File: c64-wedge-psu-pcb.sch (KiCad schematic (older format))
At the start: 15 parts, among them U1 LM2576T-5

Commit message: Make R1 pads bigger
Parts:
- R1: footprint Resistor_THT:R_Axial_DIN0207_L6.3mm_D2.5mm_P7.62mm_Horizontal -> Resistor_THT:R_Axial_DIN0411_L9.9mm_D3.6mm_P7.62mm_Vertical
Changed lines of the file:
@@
 F 0 "R1" V 5543 3650 50  0000 C CNN
 F 1 "0R" V 5634 3650 50  0000 C CNN
-F 2 "Resistor_THT:R_Axial_DIN0207_L6.3mm_D2.5mm_P7.62mm_Horizontal" V 5680 3650 50  0001 C CNN
+F 2 "Resistor_THT:R_Axial_DIN0411_L9.9mm_D3.6mm_P7.62mm_Vertical" V 5680 3650 50  0001 C CNN
 F 3 "~" H 5750 3650 50  0001 C CNN
 	1    5750 3650

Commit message: relayout, change some values and footprints
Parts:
- C1, C2: footprint Capacitor_THT:CP_Radial_D18.0mm_P7.50mm -> Capacitor_THT:CP_Radial_D16.0mm_P7.50mm
- C3: footprint Capacitor_THT:CP_Radial_D6.3mm_P2.50mm -> Capacitor_THT:CP_Radial_D8.0mm_P3.50mm
- L2: renamed from L3; value 22uH -> 20uH; footprint Inductor_THT:L_Toroid_Vertical_L19.1mm_W8.1mm_P7.10mm_Bourns_5700 -> Inductor_THT:L_Toroid_Vertical_L16.0mm_W8.0mm_P7.62mm
- R1: footprint Resistor_THT:R_Axial_DIN0411_L9.9mm_D3.6mm_P7.62mm_Vertical -> Resistor_THT:R_Axial_DIN0411_L9.9mm_D3.6mm_P5.08mm_Vertical
- U1: footprint Package_TO_SOT_THT:TO-220-5_P3.4x3.8mm_StaggerEven_Lead7.13mm_TabDown -> Package_TO_SOT_THT:TO-220-5_P3.4x3.7mm_StaggerEven_Lead3.8mm_Vertical
- renumbered L2 to L1
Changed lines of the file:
@@
 F 0 "U1" H 4600 4117 50  0000 C CNN
 F 1 "LM2576T-5" H 4600 4026 50  0000 C CNN
-F 2 "Package_TO_SOT_THT:TO-220-5_P3.4x3.8mm_StaggerEven_Lead7.13mm_TabDown" H 4600 3500 50  0001 L CIN
+F 2 "Package_TO_SOT_THT:TO-220-5_P3.4x3.7mm_StaggerEven_Lead3.8mm_Vertical" H 4600 3500 50  0001 L CIN
 F 3 "http://www.ti.com/lit/ds/symlink/lm2576.pdf" H 4600 3750 50  0001 C CNN
 	1    4600 3750
@@
 $EndComp
 $Comp
-L Device:L L2
+L Device:L L1
 U 1 1 5F7EB0E4
 P 5750 3850
-F 0 "L2" V 5662 3850 50  0000 C CNN
+F 0 "L1" V 5662 3850 50  0000 C CNN
 F 1 "150uH" V 5571 3850 50  0000 C CNN
 F 2 "Inductor_THT:L_Toroid_Vertical_L24.6mm_W15.5mm_P11.44mm_Pulse_KM-4" H 5750 3850 50  0001 C CNN
@@
 F 0 "C2" H 6218 4046 50  0000 L CNN
 F 1 "2200uF" H 6218 3955 50  0000 L CNN
-F 2 "Capacitor_THT:CP_Radial_D18.0mm_P7.50mm" H 6138 3850 50  0001 C CNN
+F 2 "Capacitor_THT:CP_Radial_D16.0mm_P7.50mm" H 6138 3850 50  0001 C CNN
 F 3 "~" H 6100 4000 50  0001 C CNN
 	1    6100 4000
@@
 F 0 "R1" V 5543 3650 50  0000 C CNN
 F 1 "0R" V 5634 3650 50  0000 C CNN
-F 2 "Resistor_THT:R_Axial_DIN0411_L9.9mm_D3.6mm_P7.62mm_Vertical" V 5680 3650 50  0001 C CNN
+F 2 "Resistor_THT:R_Axial_DIN0411_L9.9mm_D3.6mm_P5.08mm_Vertical" V 5680 3650 50  0001 C CNN
 F 3 "~" H 5750 3650 50  0001 C CNN
 	1    5750 3650
@@
 F 0 "C1" H 3668 3996 50  0000 L CNN
 F 1 "4700uF" H 3668 3905 50  0000 L CNN
-F 2 "Capacitor_THT:CP_Radial_D18.0mm_P7.50mm" H 3588 3800 50  0001 C CNN
+F 2 "Capacitor_THT:CP_Radial_D16.0mm_P7.50mm" H 3588 3800 50  0001 C CNN
 F 3 "~" H 3550 3950 50  0001 C CNN
 	1    3550 3950
@@
 F 0 "C3" H 7365 3996 50  0000 L CNN
 F 1 "100uF" H 7365 3905 50  0000 L CNN
-F 2 "Capacitor_THT:CP_Radial_D6.3mm_P2.50mm" H 7288 3800 50  0001 C CNN
+F 2 "Capacitor_THT:CP_Radial_D8.0mm_P3.50mm" H 7288 3800 50  0001 C CNN
 F 3 "~" H 7250 3950 50  0001 C CNN
 	1    7250 3950
@@
 $EndComp
 $Comp
-L Device:L L3
+L Device:L L2
 U 1 1 5F85825E
 P 6900 3650
-F 0 "L3" V 7090 3650 50  0000 C CNN
-F 1 "22uH" V 6999 3650 50  0000 C CNN
-F 2 "Inductor_THT:L_Toroid_Vertical_L19.1mm_W8.1mm_P7.10mm_Bourns_5700" H 6900 3650 50  0001 C CNN
+F 0 "L2" V 7090 3650 50  0000 C CNN
+F 1 "20uH" V 6999 3650 50  0000 C CNN
+F 2 "Inductor_THT:L_Toroid_Vertical_L16.0mm_W8.0mm_P7.62mm" H 6900 3650 50  0001 C CNN
 F 3 "~" H 6900 3650 50  0001 C CNN
 	1    6900 3650

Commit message: Modify footprints, add some info text, modify resistor values
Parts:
- C3: value 100uF -> 220uF 50V; symbol Device:C -> Device:CP
- R1: value 0R -> 200R
- R2: value 330R -> 200R
- U1: footprint Package_TO_SOT_THT:TO-220-5_P3.4x3.7mm_StaggerEven_Lead3.8mm_Vertical -> Package_TO_SOT_THT:TO-220-5_P3.4x3.8mm_StaggerEven_Lead7.13mm_TabDown
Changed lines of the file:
@@
 F 0 "U1" H 4600 4117 50  0000 C CNN
 F 1 "LM2576T-5" H 4600 4026 50  0000 C CNN
-F 2 "Package_TO_SOT_THT:TO-220-5_P3.4x3.7mm_StaggerEven_Lead3.8mm_Vertical" H 4600 3500 50  0001 L CIN
+F 2 "Package_TO_SOT_THT:TO-220-5_P3.4x3.8mm_StaggerEven_Lead7.13mm_TabDown" H 4600 3500 50  0001 L CIN
 F 3 "http://www.ti.com/lit/ds/symlink/lm2576.pdf" H 4600 3750 50  0001 C CNN
 	1    4600 3750
@@
 P 8250 4000
 F 0 "R2" V 8457 4000 50  0000 C CNN
-F 1 "330R" V 8366 4000 50  0000 C CNN
+F 1 "200R" V 8366 4000 50  0000 C CNN
 F 2 "Resistor_THT:R_Axial_DIN0207_L6.3mm_D2.5mm_P7.62mm_Horizontal" V 8180 4000 50  0001 C CNN
 F 3 "~" H 8250 4000 50  0001 C CNN
@@
 $EndComp
 Wire Wire Line
-	7250 4250 8450 4250
-Wire Wire Line
 	8450 3650 8450 4000
 Wire Wire Line
@@
 P 5750 3650
 F 0 "R1" V 5543 3650 50  0000 C CNN
-F 1 "0R" V 5634 3650 50  0000 C CNN
+F 1 "200R" V 5634 3650 50  0000 C CNN
 F 2 "Resistor_THT:R_Axial_DIN0411_L9.9mm_D3.6mm_P5.08mm_Vertical" V 5680 3650 50  0001 C CNN
 F 3 "~" H 5750 3650 50  0001 C CNN
@@
 	3550 3650 3550 3800
 $Comp
-L Device:C C3
+L Device:CP C3
 U 1 1 5F8576FF
-P 7250 3950
-F 0 "C3" H 7365 3996 50  0000 L CNN
-F 1 "100uF" H 7365 3905 50  0000 L CNN
-F 2 "Capacitor_THT:CP_Radial_D8.0mm_P3.50mm" H 7288 3800 50  0001 C CNN
-F 3 "~" H 7250 3950 50  0001 C CNN
-	1    7250 3950
+P 7150 3950
+F 0 "C3" H 7265 3996 50  0000 L CNN
+F 1 "220uF 50V" H 7265 3905 50  0000 L CNN
+F 2 "Capacitor_THT:CP_Radial_D8.0mm_P3.50mm" H 7188 3800 50  0001 C CNN
+F 3 "~" H 7150 3950 50  0001 C CNN
+	1    7150 3950
 	1    0    0    -1
 $EndComp
@@
 	6100 3650 6750 3650
 Connection ~ 6100 3650
-Wire Wire Line
-	7050 3650 7250 3650
-Wire Wire Line
-	7250 3800 7250 3650
-Connection ~ 7250 3650
-Wire Wire Line
-	7250 3650 8450 3650
-Wire Wire Line
-	7250 4100 7250 4250
-Wire Wire Line
-	7250 4250 6100 4250
-Connection ~ 7250 4250
 Connection ~ 6100 4250
 Wire Notes Line
@@
 	3250 3650 3550 3650
 Connection ~ 3550 3650
+Wire Wire Line
+	7050 3650 7150 3650
+Wire Wire Line
+	6100 4250 7150 4250
+Wire Wire Line
+	7150 3800 7150 3650
+Connection ~ 7150 3650
+Wire Wire Line
+	7150 3650 8450 3650
+Wire Wire Line
+	7150 4100 7150 4250
+Connection ~ 7150 4250
+Wire Wire Line
+	7150 4250 8450 4250
 $EndSCHEMATC

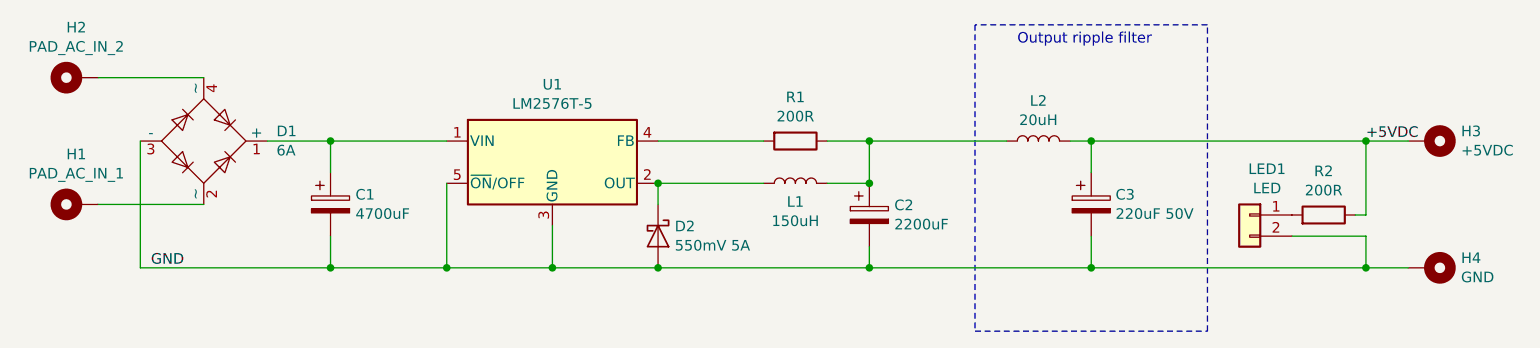
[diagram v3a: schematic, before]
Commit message: V1.1: Proper voltage divider to Feedback line. Make tracks wider. Some relayout. Update resistor values and L2 value.
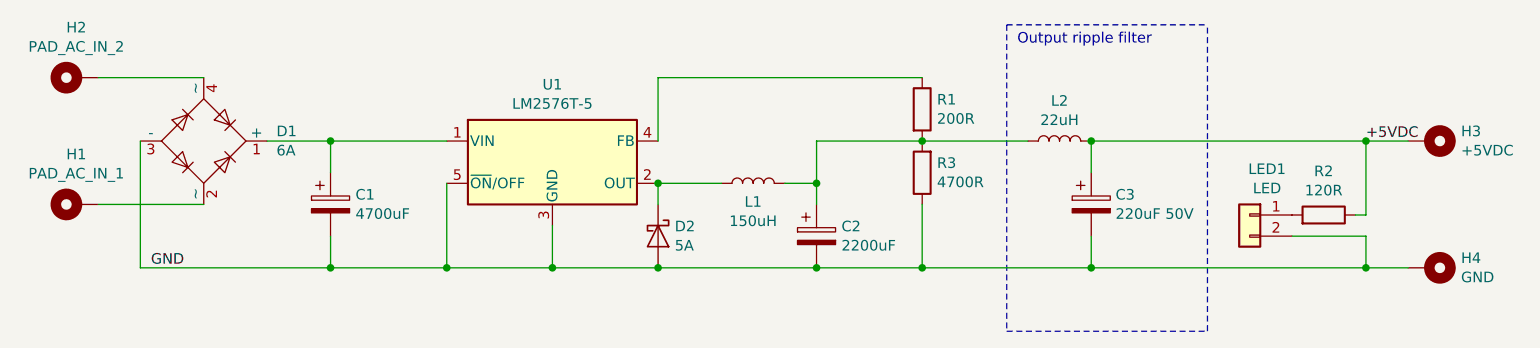
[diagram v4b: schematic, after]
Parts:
- added R3: 4700R, Resistor_THT:R_Axial_DIN0207_L6.3mm_D2.5mm_P2.54mm_Vertical, symbol Device:R
- D2: value 550mV 5A -> 5A
- L2: value 20uH -> 22uH
- R1: footprint Resistor_THT:R_Axial_DIN0411_L9.9mm_D3.6mm_P5.08mm_Vertical -> Resistor_THT:R_Axial_DIN0207_L6.3mm_D2.5mm_P2.54mm_Vertical
- R2: value 200R -> 120R; footprint Resistor_THT:R_Axial_DIN0207_L6.3mm_D2.5mm_P7.62mm_Horizontal -> Resistor_THT:R_Axial_DIN0207_L6.3mm_D2.5mm_P2.54mm_Vertical
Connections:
- net GND: now also R3.1
- net at U1.4 (FB): now also R1.1; no longer R1.2
- net at C2.1, L1.2, L2.1: now also R1.2, R3.2; no longer R1.1
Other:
- moved on the sheet: C2, L1, L2, R1
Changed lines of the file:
@@
 Title "C64 Wedge PSU PCB"
 Date "2020-11-02"
-Rev "1.0"
+Rev "1.1"
 Comp "Timo Mömmö"
 Comment1 ""
@@
 L Device:L L1
 U 1 1 5F7EB0E4
-P 5750 3850
-F 0 "L1" V 5662 3850 50  0000 C CNN
-F 1 "150uH" V 5571 3850 50  0000 C CNN
-F 2 "Inductor_THT:L_Toroid_Vertical_L24.6mm_W15.5mm_P11.44mm_Pulse_KM-4" H 5750 3850 50  0001 C CNN
-F 3 "~" H 5750 3850 50  0001 C CNN
-	1    5750 3850
+P 5550 3850
+F 0 "L1" V 5462 3850 50  0000 C CNN
+F 1 "150uH" V 5371 3850 50  0000 C CNN
+F 2 "Inductor_THT:L_Toroid_Vertical_L24.6mm_W15.5mm_P11.44mm_Pulse_KM-4" H 5550 3850 50  0001 C CNN
+F 3 "~" H 5550 3850 50  0001 C CNN
+	1    5550 3850
 	0    -1   -1   0
 $EndComp
@@
 P 5100 4100
 F 0 "D2" V 5054 4179 50  0000 L CNN
-F 1 "550mV 5A" V 5145 4179 50  0000 L CNN
+F 1 "5A" V 5145 4179 50  0000 L CNN
 F 2 "Diode_THT:D_DO-201AD_P12.70mm_Horizontal" H 5100 4100 50  0001 C CNN
 F 3 "~" H 5100 4100 50  0001 C CNN
@@
 L Device:CP C2
 U 1 1 5F7ED9FD
-P 6100 4000
-F 0 "C2" H 6218 4046 50  0000 L CNN
-F 1 "2200uF" H 6218 3955 50  0000 L CNN
-F 2 "Capacitor_THT:CP_Radial_D16.0mm_P7.50mm" H 6138 3850 50  0001 C CNN
-F 3 "~" H 6100 4000 50  0001 C CNN
-	1    6100 4000
-	1    0    0    -1
-$EndComp
-Wire Wire Line
-	6100 3650 6100 3850
-Wire Wire Line
-	6100 4150 6100 4250
+P 5850 4100
+F 0 "C2" H 5968 4146 50  0000 L CNN
+F 1 "2200uF" H 5968 4055 50  0000 L CNN
+F 2 "Capacitor_THT:CP_Radial_D16.0mm_P7.50mm" H 5888 3950 50  0001 C CNN
+F 3 "~" H 5850 4100 50  0001 C CNN
+	1    5850 4100
+	1    0    0    -1
+$EndComp
 $Comp
 L Mechanical:MountingHole_Pad H1
@@
 P 8250 4000
 F 0 "R2" V 8457 4000 50  0000 C CNN
-F 1 "200R" V 8366 4000 50  0000 C CNN
-F 2 "Resistor_THT:R_Axial_DIN0207_L6.3mm_D2.5mm_P7.62mm_Horizontal" V 8180 4000 50  0001 C CNN
+F 1 "120R" V 8366 4000 50  0000 C CNN
+F 2 "Resistor_THT:R_Axial_DIN0207_L6.3mm_D2.5mm_P2.54mm_Vertical" V 8180 4000 50  0001 C CNN
 F 3 "~" H 8250 4000 50  0001 C CNN
 	1    8250 4000
@@
 L Device:R R1
 U 1 1 5F81F757
-P 5750 3650
-F 0 "R1" V 5543 3650 50  0000 C CNN
-F 1 "200R" V 5634 3650 50  0000 C CNN
-F 2 "Resistor_THT:R_Axial_DIN0411_L9.9mm_D3.6mm_P5.08mm_Vertical" V 5680 3650 50  0001 C CNN
-F 3 "~" H 5750 3650 50  0001 C CNN
-	1    5750 3650
-	0    1    1    0
+P 6350 3500
+F 0 "R1" H 6420 3546 50  0000 L CNN
+F 1 "200R" H 6420 3455 50  0000 L CNN
+F 2 "Resistor_THT:R_Axial_DIN0207_L6.3mm_D2.5mm_P2.54mm_Vertical" V 6280 3500 50  0001 C CNN
+F 3 "~" H 6350 3500 50  0001 C CNN
+	1    6350 3500
+	1    0    0    -1
 $EndComp
 Wire Wire Line
@@
 Wire Wire Line
 	5100 3850 5100 3950
-Wire Wire Line
-	5100 3850 5600 3850
-Connection ~ 5100 3850
-Wire Wire Line
-	5100 3650 5600 3650
-Wire Wire Line
-	5900 3650 6100 3650
-Wire Wire Line
-	5900 3850 6100 3850
-Connection ~ 6100 3850
-Wire Wire Line
-	5100 4250 6100 4250
 Connection ~ 5100 4250
 $Comp
@@
 L Device:L L2
 U 1 1 5F85825E
-P 6900 3650
-F 0 "L2" V 7090 3650 50  0000 C CNN
-F 1 "20uH" V 6999 3650 50  0000 C CNN
-F 2 "Inductor_THT:L_Toroid_Vertical_L16.0mm_W8.0mm_P7.62mm" H 6900 3650 50  0001 C CNN
-F 3 "~" H 6900 3650 50  0001 C CNN
-	1    6900 3650
-	0    -1   -1   0
-$EndComp
-Wire Wire Line
-	6100 3650 6750 3650
-Connection ~ 6100 3650
-Connection ~ 6100 4250
-Wire Notes Line
-	6600 3100 6600 4550
-Wire Notes Line
-	6600 4550 7700 4550
+P 7000 3650
+F 0 "L2" V 7190 3650 50  0000 C CNN
+F 1 "22uH" V 7099 3650 50  0000 C CNN
+F 2 "Inductor_THT:L_Toroid_Vertical_L16.0mm_W8.0mm_P7.62mm" H 7000 3650 50  0001 C CNN
+F 3 "~" H 7000 3650 50  0001 C CNN
+	1    7000 3650
+	0    -1   -1   0
+$EndComp
+Wire Notes Line
+	6750 3100 6750 4550
 Wire Notes Line
 	7700 4550 7700 3100
-Wire Notes Line
-	7700 3100 6600 3100
 Text Notes 6800 3200 0    50   ~ 0
 Output ripple filter
@@
 Connection ~ 3550 3650
 Wire Wire Line
-	7050 3650 7150 3650
-Wire Wire Line
-	6100 4250 7150 4250
-Wire Wire Line
 	7150 3800 7150 3650
 Connection ~ 7150 3650
@@
 Wire Wire Line
 	7150 4250 8450 4250
+Wire Wire Line
+	5100 4250 5850 4250
+Connection ~ 5850 4250
+Wire Wire Line
+	5100 3850 5400 3850
+Connection ~ 5100 3850
+Wire Wire Line
+	5700 3850 5850 3850
+Wire Wire Line
+	5850 3850 5850 3950
+$Comp
+L Device:R R3
+U 1 1 5FBCC66C
+P 6350 3800
+F 0 "R3" H 6280 3754 50  0000 R CNN
+F 1 "4700R" H 6280 3845 50  0000 R CNN
+F 2 "Resistor_THT:R_Axial_DIN0207_L6.3mm_D2.5mm_P2.54mm_Vertical" V 6280 3800 50  0001 C CNN
+F 3 "~" H 6350 3800 50  0001 C CNN
+	1    6350 3800
+	-1   0    0    1
+$EndComp
+Wire Notes Line
+	6750 3100 7700 3100
+Wire Notes Line
+	6750 4550 7700 4550
+Wire Wire Line
+	6350 3650 6850 3650
+Connection ~ 6350 3650
+Wire Wire Line
+	5850 3850 5850 3650
+Wire Wire Line
+	5850 3650 6350 3650
+Wire Wire Line
+	5850 4250 6350 4250
+Connection ~ 5850 3850
+Wire Wire Line
+	6350 3950 6350 4250
+Connection ~ 6350 4250
+Wire Wire Line
+	6350 4250 7150 4250
+Wire Wire Line
+	6350 3350 5100 3350
+Wire Wire Line
+	5100 3350 5100 3650
 $EndSCHEMATC

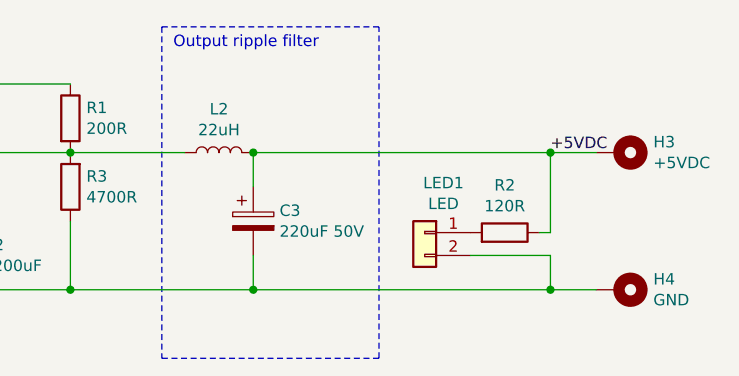
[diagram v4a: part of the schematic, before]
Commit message: update resistor values
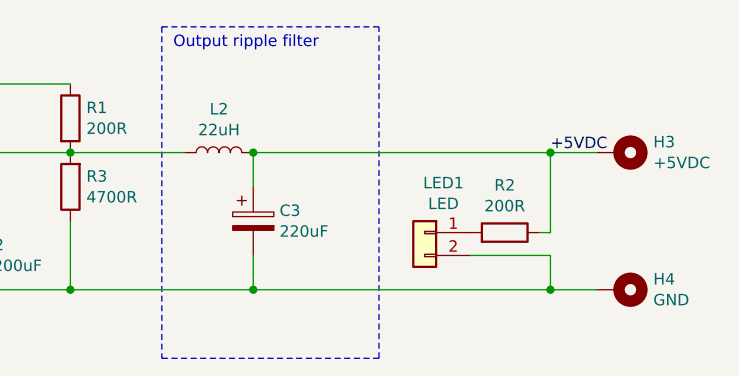
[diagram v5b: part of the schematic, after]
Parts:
- C3: value 220uF 50V -> 220uF
- R2: value 120R -> 200R
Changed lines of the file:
@@
 P 8250 4000
 F 0 "R2" V 8457 4000 50  0000 C CNN
-F 1 "120R" V 8366 4000 50  0000 C CNN
+F 1 "200R" V 8366 4000 50  0000 C CNN
 F 2 "Resistor_THT:R_Axial_DIN0207_L6.3mm_D2.5mm_P2.54mm_Vertical" V 8180 4000 50  0001 C CNN
 F 3 "~" H 8250 4000 50  0001 C CNN
@@
 P 7150 3950
 F 0 "C3" H 7265 3996 50  0000 L CNN
-F 1 "220uF 50V" H 7265 3905 50  0000 L CNN
+F 1 "220uF" H 7265 3905 50  0000 L CNN
 F 2 "Capacitor_THT:CP_Radial_D8.0mm_P3.50mm" H 7188 3800 50  0001 C CNN
 F 3 "~" H 7150 3950 50  0001 C CNN

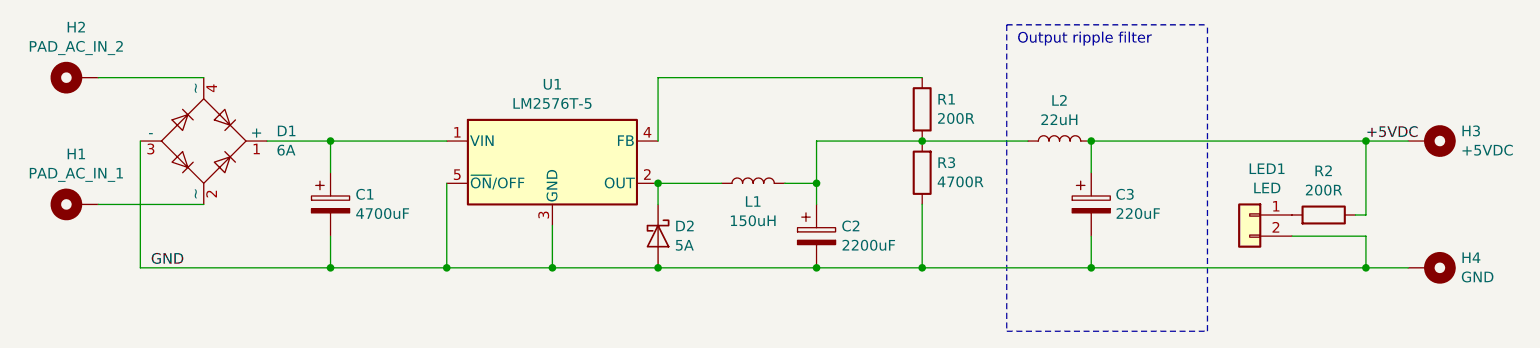
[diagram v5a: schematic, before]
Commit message: Fix feedback voltage divider (issue #1). Also change resitors to horizontal orientation.
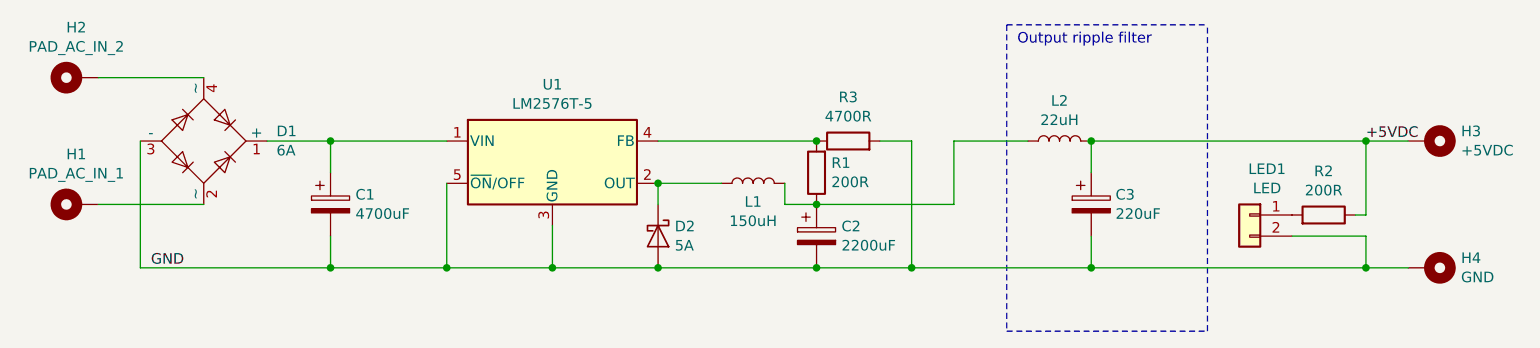
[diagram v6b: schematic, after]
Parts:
- LED1: footprint Connector_PinHeader_2.54mm:PinHeader_1x02_P2.54mm_Vertical -> LED_THT:LED_D3.0mm
- R1, R2, R3: footprint Resistor_THT:R_Axial_DIN0207_L6.3mm_D2.5mm_P2.54mm_Vertical -> Resistor_THT:R_Axial_DIN0207_L6.3mm_D2.5mm_P7.62mm_Horizontal
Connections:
- net GND: now also R3.2; no longer R3.1
- net at U1.4 (FB): now also R1.2, R3.1; no longer R1.1
- net at C2.1, L1.2, L2.1: now also R1.1; no longer R1.2, R3.2
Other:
- moved on the sheet: R1, R3
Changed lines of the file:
@@
 Sheet 1 1
 Title "C64 Wedge PSU PCB"
-Date "2020-11-02"
-Rev "1.1"
+Date "2022-01-30"
+Rev "1.2"
 Comp "Timo Mömmö"
 Comment1 ""
@@
 F 0 "R2" V 8457 4000 50  0000 C CNN
 F 1 "200R" V 8366 4000 50  0000 C CNN
-F 2 "Resistor_THT:R_Axial_DIN0207_L6.3mm_D2.5mm_P2.54mm_Vertical" V 8180 4000 50  0001 C CNN
+F 2 "Resistor_THT:R_Axial_DIN0207_L6.3mm_D2.5mm_P7.62mm_Horizontal" V 8180 4000 50  0001 C CNN
 F 3 "~" H 8250 4000 50  0001 C CNN
 	1    8250 4000
@@
 F 0 "LED1" H 7818 4217 50  0000 C CNN
 F 1 "LED" H 7818 4126 50  0000 C CNN
-F 2 "Connector_PinHeader_2.54mm:PinHeader_1x02_P2.54mm_Vertical" H 7900 4000 50  0001 C CNN
+F 2 "LED_THT:LED_D3.0mm" H 7900 4000 50  0001 C CNN
 F 3 "~" H 7900 4000 50  0001 C CNN
 	1    7900 4000
@@
 L Device:R R1
 U 1 1 5F81F757
-P 6350 3500
-F 0 "R1" H 6420 3546 50  0000 L CNN
-F 1 "200R" H 6420 3455 50  0000 L CNN
-F 2 "Resistor_THT:R_Axial_DIN0207_L6.3mm_D2.5mm_P2.54mm_Vertical" V 6280 3500 50  0001 C CNN
-F 3 "~" H 6350 3500 50  0001 C CNN
-	1    6350 3500
-	1    0    0    -1
+P 5850 3800
+F 0 "R1" H 5780 3754 50  0000 R CNN
+F 1 "200R" H 5780 3845 50  0000 R CNN
+F 2 "Resistor_THT:R_Axial_DIN0207_L6.3mm_D2.5mm_P7.62mm_Horizontal" V 5780 3800 50  0001 C CNN
+F 3 "~" H 5850 3800 50  0001 C CNN
+	1    5850 3800
+	-1   0    0    1
 $EndComp
 Wire Wire Line
@@
 	5100 3850 5400 3850
 Connection ~ 5100 3850
-Wire Wire Line
-	5700 3850 5850 3850
-Wire Wire Line
-	5850 3850 5850 3950
 $Comp
 L Device:R R3
 U 1 1 5FBCC66C
-P 6350 3800
-F 0 "R3" H 6280 3754 50  0000 R CNN
-F 1 "4700R" H 6280 3845 50  0000 R CNN
-F 2 "Resistor_THT:R_Axial_DIN0207_L6.3mm_D2.5mm_P2.54mm_Vertical" V 6280 3800 50  0001 C CNN
-F 3 "~" H 6350 3800 50  0001 C CNN
-	1    6350 3800
-	-1   0    0    1
+P 6000 3650
+F 0 "R3" V 6207 3650 50  0000 C CNN
+F 1 "4700R" V 6116 3650 50  0000 C CNN
+F 2 "Resistor_THT:R_Axial_DIN0207_L6.3mm_D2.5mm_P7.62mm_Horizontal" V 5930 3650 50  0001 C CNN
+F 3 "~" H 6000 3650 50  0001 C CNN
+	1    6000 3650
+	0    -1   -1   0
 $EndComp
 Wire Notes Line
@@
 	6750 4550 7700 4550
 Wire Wire Line
-	6350 3650 6850 3650
-Connection ~ 6350 3650
-Wire Wire Line
-	5850 3850 5850 3650
-Wire Wire Line
-	5850 3650 6350 3650
-Wire Wire Line
-	5850 4250 6350 4250
-Connection ~ 5850 3850
-Wire Wire Line
-	6350 3950 6350 4250
-Connection ~ 6350 4250
-Wire Wire Line
-	6350 4250 7150 4250
-Wire Wire Line
-	6350 3350 5100 3350
-Wire Wire Line
-	5100 3350 5100 3650
+	5700 3850 5700 3950
+Wire Wire Line
+	5700 3950 5850 3950
+Connection ~ 5850 3950
+Wire Wire Line
+	5100 3650 5850 3650
+Connection ~ 5850 3650
+Wire Wire Line
+	5850 4250 6300 4250
+Wire Wire Line
+	6150 3650 6300 3650
+Wire Wire Line
+	6300 3650 6300 4250
+Connection ~ 6300 4250
+Wire Wire Line
+	6300 4250 7150 4250
+Wire Wire Line
+	5850 3950 6500 3950
+Wire Wire Line
+	6500 3950 6500 3650
+Wire Wire Line
+	6500 3650 6850 3650
 $EndSCHEMATC
